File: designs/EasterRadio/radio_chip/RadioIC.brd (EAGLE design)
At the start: 38 x 29 mm, 26 parts, among them J1 S2B-NSHSS-TB, J2 S2B-NSHSS-TB, Q1 2SC3838T146, Y1 32.768kHz crystal

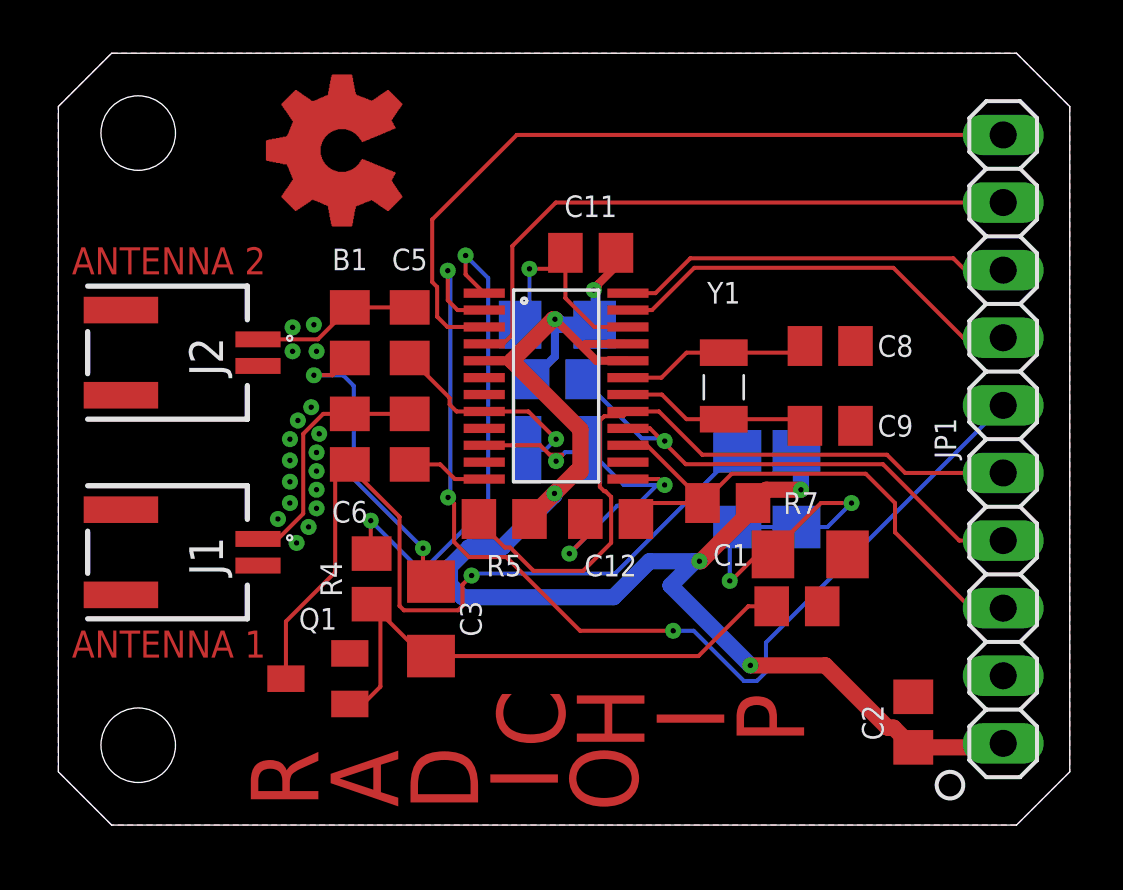
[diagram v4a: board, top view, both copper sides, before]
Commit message: added new design of radio parts slide change naming on mainboard and routing on radio ic
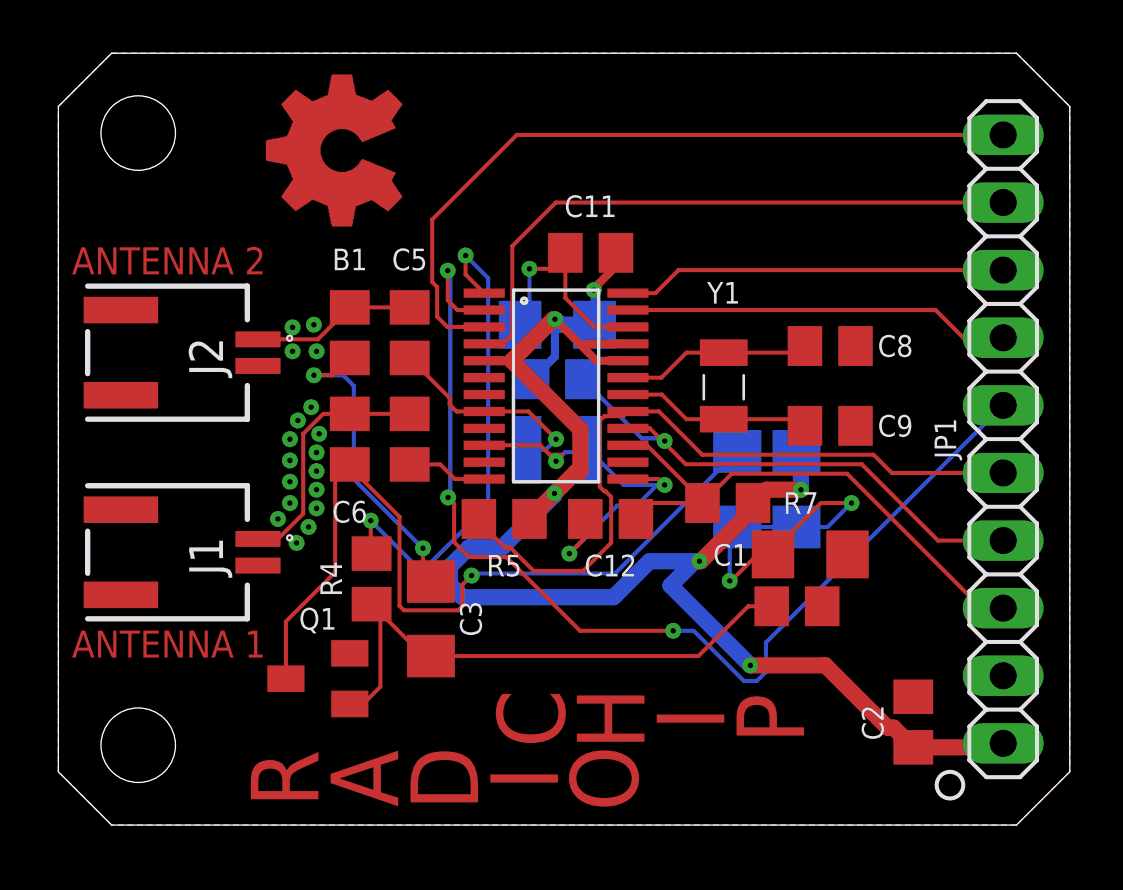
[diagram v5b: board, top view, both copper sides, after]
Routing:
- net ROUT: track 15.8 -> 14.5 mm
- net RST: track 21.0 -> 20.3 mm
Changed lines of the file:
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@@
 <contactref element="SI4844-A101" pad="SDIO"/>
 <contactref element="JP1" pad="7"/>
-<wire x1="33.85064375" y1="10.69" x2="30.98324375" y2="13.5574" width="0.1524" layer="1"/>
+<wire x1="33.05064375" y1="10.69" x2="30.18324375" y2="13.5574" width="0.1524" layer="1"/>
 <wire x1="22.224996875" y1="14.905" x2="21.4" y2="14.905" width="0.1524" layer="1"/>
 <wire x1="23.572596875" y1="13.5574" x2="22.789996875" y2="14.34" width="0.1524" layer="1"/>
 <wire x1="22.789996875" y1="14.34" x2="22.224996875" y2="14.905" width="0.1524" layer="1"/>
-<wire x1="35.5" y1="10.69" x2="33.85064375" y2="10.69" width="0.1524" layer="1"/>
-<wire x1="30.98324375" y1="13.5574" x2="23.572596875" y2="13.5574" width="0.1524" layer="1"/>
+<wire x1="35.5" y1="10.69" x2="33.05064375" y2="10.69" width="0.1524" layer="1"/>
+<wire x1="30.18324375" y1="13.5574" x2="23.572596875" y2="13.5574" width="0.1524" layer="1"/>
 <wire x1="19.7" y1="16.75" x2="21.920428125" y2="14.529571875" width="0.1524" layer="16"/>
 <wire x1="22.679571875" y1="14.529571875" x2="22.779571875" y2="14.429571875" width="0.1524" layer="16"/>
@@
 <contactref element="SI4844-A101" pad="!RST"/>
 <contactref element="JP1" pad="8"/>
-<wire x1="35.5" y1="8.15" x2="34.2865125" y2="8.15" width="0.1524" layer="1"/>
-<wire x1="34.2865125" y1="8.15" x2="31.4352" y2="11.0013125" width="0.1524" layer="1"/>
-<wire x1="31.4352" y1="11.0013125" x2="31.4352" y2="12.1" width="0.1524" layer="1"/>
-<wire x1="31.4352" y1="12.1" x2="30.3352" y2="13.2" width="0.1524" layer="1"/>
-<wire x1="30.3352" y1="13.2" x2="25.3" y2="13.2" width="0.1524" layer="1"/>
+<wire x1="35.5" y1="8.15" x2="34.6852" y2="8.15" width="0.1524" layer="1"/>
+<wire x1="34.6852" y1="8.15" x2="29.6352" y2="13.2" width="0.1524" layer="1"/>
+<wire x1="29.6352" y1="13.2" x2="25.3" y2="13.2" width="0.1524" layer="1"/>
 <wire x1="25.3" y1="13.2" x2="24.2" y2="12.1" width="0.1524" layer="1"/>
 <wire x1="24.2" y1="12.1" x2="24.2" y2="12.182675" width="0.1524" layer="1"/>
@@
 <contactref element="SI4844-A101" pad="SCLK"/>
 <contactref element="JP1" pad="6"/>
-<wire x1="35.5" y1="13.23" x2="31.8160875" y2="13.23" width="0.1524" layer="1"/>
-<wire x1="31.8160875" y1="13.23" x2="31.1312875" y2="13.9148" width="0.1524" layer="1"/>
+<wire x1="35.5" y1="13.23" x2="31.3160875" y2="13.23" width="0.1524" layer="1"/>
+<wire x1="31.3160875" y1="13.23" x2="30.6312875" y2="13.9148" width="0.1524" layer="1"/>
 <wire x1="22.5666625" y1="15.54" x2="21.4" y2="15.54" width="0.1524" layer="1"/>
 <wire x1="24.1918625" y1="13.9148" x2="22.5666625" y2="15.54" width="0.1524" layer="1"/>
-<wire x1="31.1312875" y1="13.9148" x2="24.1918625" y2="13.9148" width="0.1524" layer="1"/>
+<wire x1="30.6312875" y1="13.9148" x2="24.1918625" y2="13.9148" width="0.1524" layer="1"/>
 <wire x1="20.508525" y1="12.5438" x2="20.3438" y2="12.708525" width="0.1524" layer="1"/>
 <wire x1="20.3438" y1="15.196475" x2="20.508525" y2="15.3612" width="0.1524" layer="1"/>
@@
 <contactref element="JP1" pad="4"/>
 <wire x1="35.5" y1="18.31" x2="34" y2="18.31" width="0.1524" layer="1"/>
-<wire x1="34" y1="18.31" x2="31.3726" y2="20.9374" width="0.1524" layer="1"/>
-<wire x1="31.3726" y1="20.9374" x2="23.89284375" y2="20.9374" width="0.1524" layer="1"/>
-<wire x1="22.30544375" y1="19.35" x2="21.4" y2="19.35" width="0.1524" layer="1"/>
-<wire x1="23.89284375" y1="20.9374" x2="22.30544375" y2="19.35" width="0.1524" layer="1"/>
+<wire x1="34" y1="18.31" x2="32.96" y2="19.35" width="0.1524" layer="1"/>
+<wire x1="32.96" y1="19.35" x2="21.4" y2="19.35" width="0.1524" layer="1"/>
 </signal>
 <signal name="LOUT">
 <contactref element="SI4844-A101" pad="LOUT"/>
 <contactref element="JP1" pad="3"/>
-<wire x1="35.5" y1="20.85" x2="34.07" y2="20.85" width="0.1524" layer="1"/>
-<wire x1="34.07" y1="20.85" x2="33.6252" y2="21.2948" width="0.1524" layer="1"/>
-<wire x1="33.6252" y1="21.2948" x2="23.7448" y2="21.2948" width="0.1524" layer="1"/>
+<wire x1="35.5" y1="20.85" x2="23.3" y2="20.85" width="0.1524" layer="1"/>
 <wire x1="22.435" y1="19.985" x2="21.4" y2="19.985" width="0.1524" layer="1"/>
-<wire x1="23.7448" y1="21.2948" x2="22.435" y2="19.985" width="0.1524" layer="1"/>
+<wire x1="23.3" y1="20.85" x2="22.435" y2="19.985" width="0.1524" layer="1"/>
 </signal>
 <signal name="DBYP">
